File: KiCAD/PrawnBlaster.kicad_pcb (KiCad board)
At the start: 2 copper layers, 135 x 76.2 mm, 30 parts, among them J1 DB9_Female, J11 Flag_12, J14 Conn_01x03, J2 Flag_15, J5 Flag_14, J8 Flag_13, Q1 DMP6023LE, U1 78L05, U2 74ABT245

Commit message: Add 64Pin Case Power Supply, update PCB dimensions and SMA-Type
Note: Pi Pico footprint is missing!
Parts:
- removed H2: MountingHole, MountingHole:MountingHole_2.7mm_M2.5_DIN965
- removed J11: Flag_12, Connector_Coaxial:SMA_Amphenol_132134_Vertical
- removed J14: Conn_01x03, Connector:FanPinHeader_1x03_P2.54mm_Vertical
- removed J8: Flag_13, Connector_Coaxial:SMA_Amphenol_132134_Vertical
- added H4: MountingHole, MountingHole:MountingHole_2.7mm_M2.5_DIN965, F.Cu at (257.2, 42.0)
- added J3: Flag_14, Connector_Coaxial:SMA_Amphenol_132289_EdgeMount, F.Cu at (271.4, 20.6)
- added J4: Flag_13, Connector_Coaxial:SMA_Amphenol_132289_EdgeMount, F.Cu at (271.4, 32.8)
- added J6: C64AC, Custom_footprints_project:Socket_DIN41612-CaseC1-AC-Male-64Pin-2rows, F.Cu at (296.0, -37.6)
- added U2: SN74LV1T34DBV, Package_TO_SOT_SMD:SOT-23-5, F.Cu at (269.1, 41.2)
- J1: value DB9_Female -> Conn_Coaxial; footprint Connector_Dsub:DSUB-9_Female_Vertical_P2.77x2.84mm -> Connector_Coaxial:SMA_Amphenol_132289_EdgeMount
- J2: value Flag_15 -> Flag_12; footprint Connector_Coaxial:SMA_Amphenol_132134_Vertical -> Connector_Coaxial:SMA_Amphenol_132289_EdgeMount
- J5: value Flag_14 -> Flag_12; footprint Connector_Coaxial:SMA_Amphenol_132134_Vertical -> Connector_Coaxial:SMA_Amphenol_132289_EdgeMount
- moved J1 210.9 mm to (252.1, 20.6), turned to 0 degrees
- moved J5 162.9 mm to (290.7, 20.6)
- moved J2 116.1 mm to (252.1, 32.8)
- moved C1 57.4 mm to (76.7, -1.00)
- moved C2 57.4 mm to (76.7, 3.50)
- moved C3 57.4 mm to (77.7, 14.5)
- moved C4 57.4 mm to (76.7, 11.5)
- moved D1 57.4 mm to (84.7, 0.50)
- moved D2 57.4 mm to (70.2, 1.00)
- moved Q1 57.4 mm to (63.2, 1.50)
- moved R1 57.4 mm to (91.8, 25.4)
- moved R2 57.4 mm to (91.8, 22.9)
- moved R3 57.4 mm to (91.8, 20.4)
- moved R4 57.4 mm to (91.8, 17.9)
- moved R5 57.4 mm to (71.1, 4.00)
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- renumbered C5 to C4, H3 to H5, H4 to H7, R13 to R5, R14 to R6, R16 to R7, R18 to R8, R20 to R9, U1 to U3, U2 to U4
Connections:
- J1 pad 1: GND -> Net-(J1-Pad1)
- R1 pad 2: Net-(J11-Pad1) -> Net-(J5-Pad1)
- R3 pad 2: Net-(J5-Pad1) -> Net-(J3-Pad1)
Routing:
- net Net-(J2-Pad1): track 77.2 -> 0.00 mm
- net Net-(J5-Pad1): track 66.1 -> 0.00 mm
- net Net-(J6-Pad1): track 65.6 -> 0.00 mm, vias 2 -> 0
- net Net-(J4-Pad1): track 55.7 -> 0.00 mm
- net Net-(J9-Pad1): track 54.4 -> 0.00 mm
- net Net-(J3-Pad1): track 44.3 -> 0.00 mm
- net /Output Buffer/Vcc: track 109.9 -> 67.4 mm
- net /Output Buffer/A11: track 41.5 -> 0.00 mm
- net /Output Buffer/A10: track 41.1 -> 0.00 mm
- net /Output Buffer/A8: track 40.5 -> 0.00 mm
- net Net-(J11-Pad1): track 40.5 -> 0.00 mm
- net /Output Buffer/A9: track 40.1 -> 0.00 mm
- net Net-(J12-Pad1): track 38.8 -> 0.00 mm
- net /Output Buffer/A6: track 37.5 -> 0.00 mm
- net /Output Buffer/A4: track 37.3 -> 0.00 mm
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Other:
- board size 135 x 76.2 mm -> 160 x 100 mm
- board text removed: "1"
- board text removed: "2"
- board text removed: "3"
- board text removed: "8-18V"
- board text removed: "GND"
- board text removed: "NC"
- board text removed: "Pin"

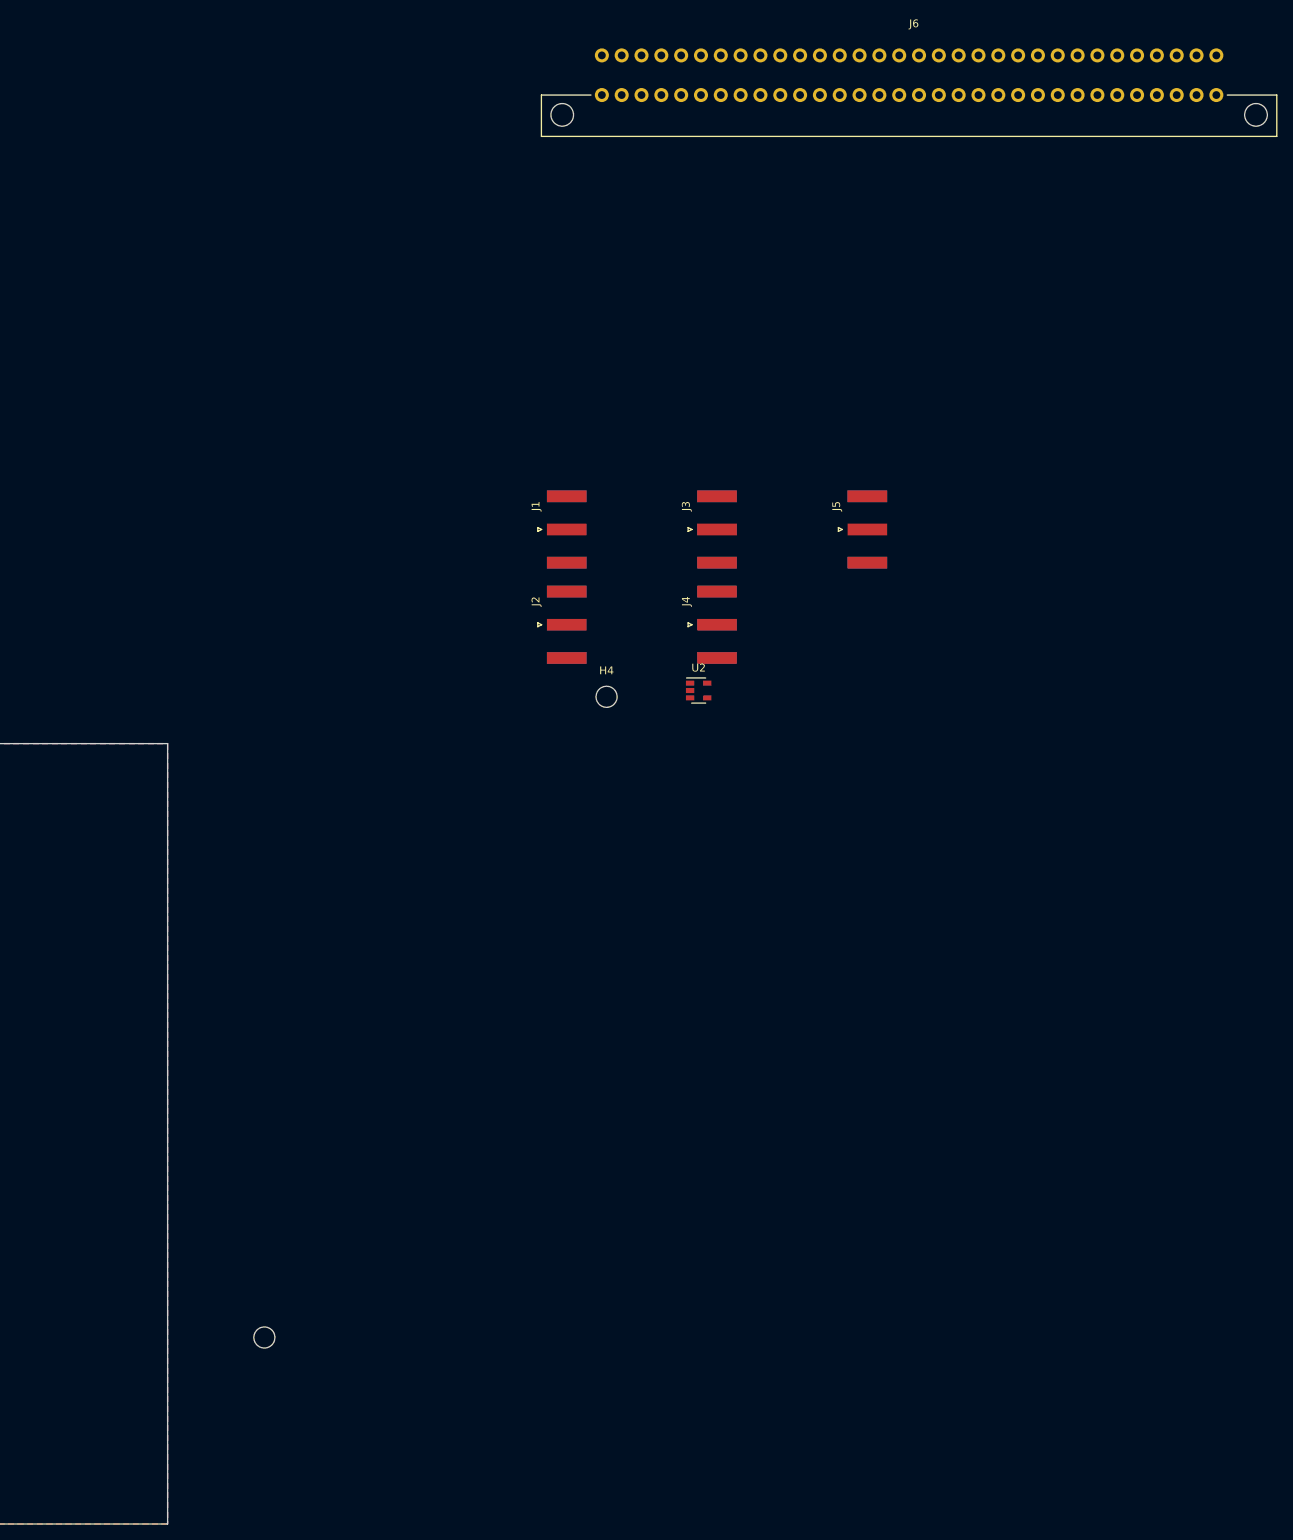
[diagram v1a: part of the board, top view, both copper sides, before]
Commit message: Place 64Pin Connector
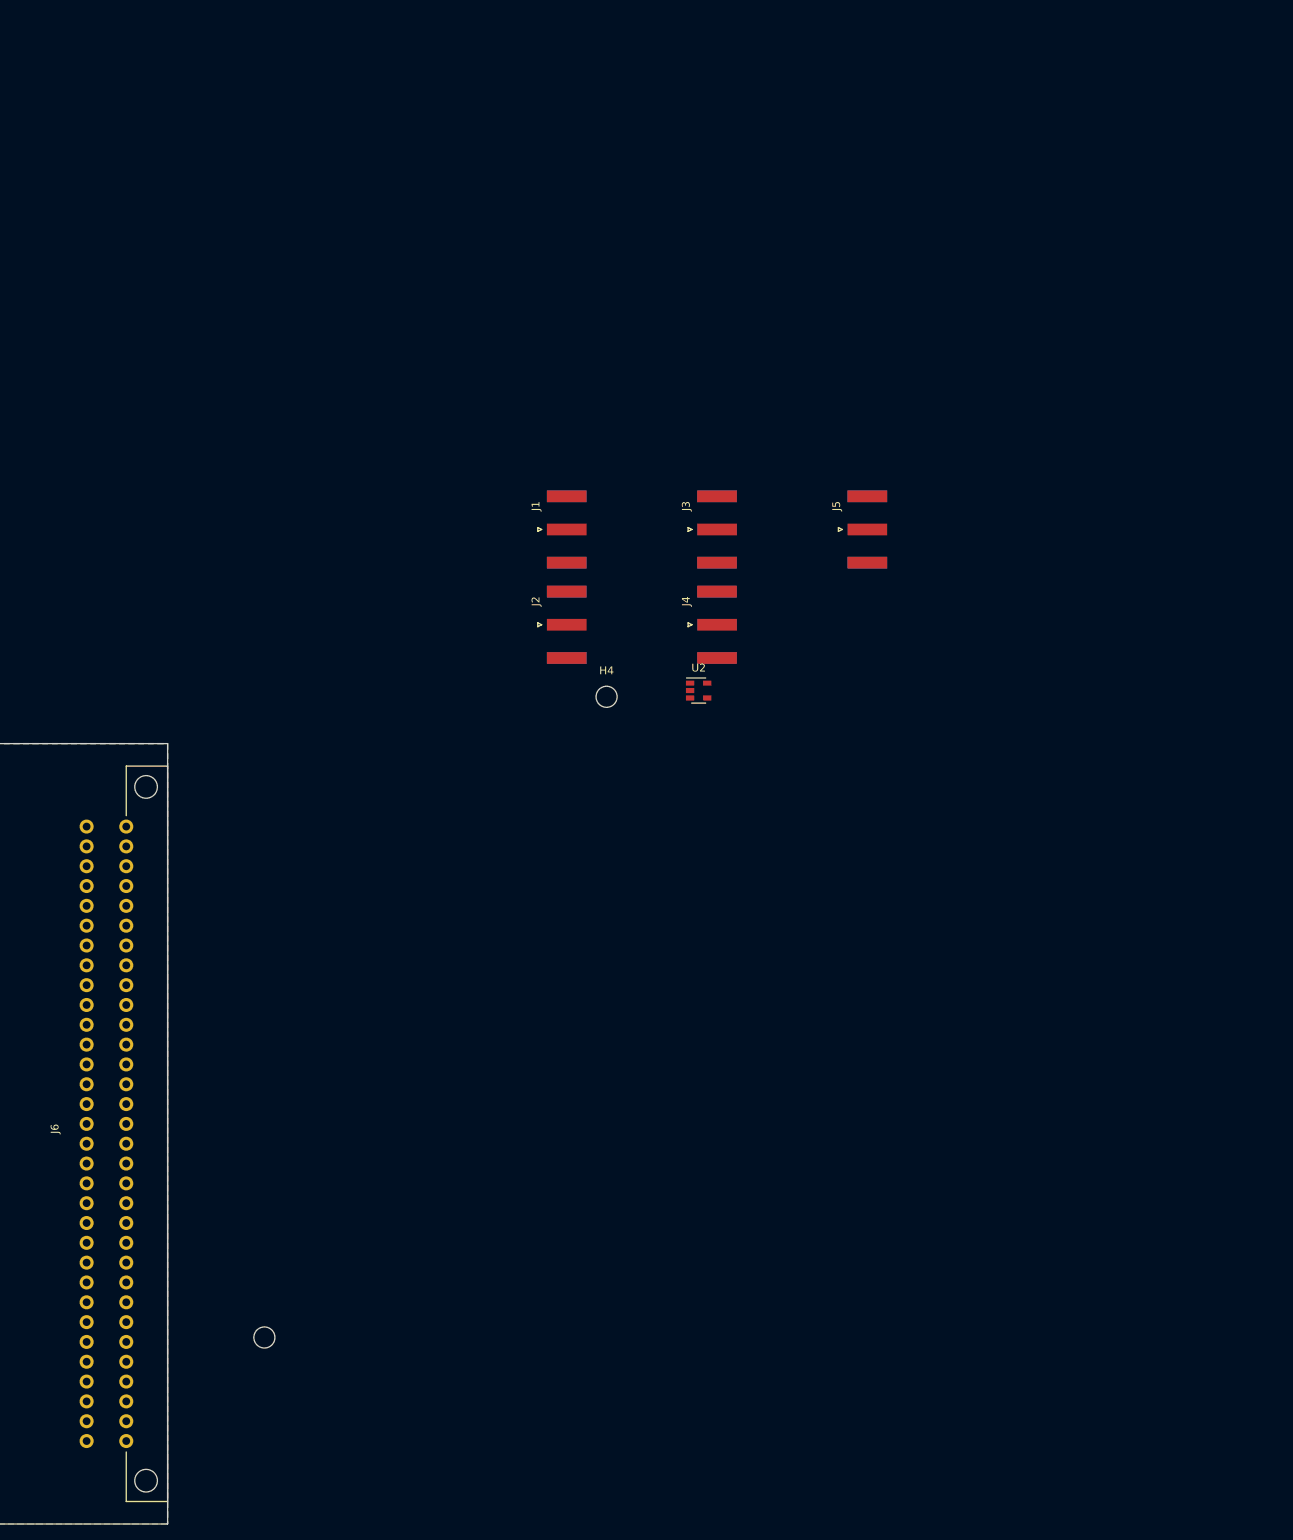
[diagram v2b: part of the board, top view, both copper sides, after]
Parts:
- moved J6 170.2 mm to (193.2, 98.0), turned to 90 degrees

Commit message: Add PiPico Footprint and route PCB without SMA connectors
Schematic was updated and routing on PCB was done except for input/output connectors.
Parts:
- added J10: Conn_01x20_Male, Connector_PinHeader_2.54mm:PinHeader_1x20_P2.54mm_Vertical, F.Cu at (118.2, 78.4)
- added J7: Conn_Coaxial, Connector_Coaxial:SMA_Amphenol_132289_EdgeMount, F.Cu at (46.9, 72.0)
- added J8: Conn_01x20_Male, Connector_PinHeader_2.54mm:PinHeader_1x20_P2.54mm_Vertical, F.Cu at (155.7, 126.6)
- added J9: Conn_01x03_Male, Connector_PinHeader_2.54mm:PinHeader_1x03_P2.54mm_Vertical, F.Cu at (134.3, 135.4)
- added U1: Pico, Custom_footprints_project:RPi_Pico_SMD_TH, F.Cu at (136.8, 102.5)
- added U5: SN74LV1T34DBV, Package_TO_SOT_SMD:SOT-23-5, F.Cu at (108.5, 72.7)
- moved J5 255.5 mm to (46.9, 97.0), turned to 180 degrees
- moved J3 246.5 mm to (46.8, 122.1), turned to 180 degrees
- moved J4 237.3 mm to (46.8, 109.3), turned to 180 degrees
- moved J2 230.2 mm to (47.0, 137.3), turned to 180 degrees
- moved J1 208.9 mm to (46.4, 56.8), turned to 180 degrees
- moved U2 164.6 mm to (108.5, 77.5)
- moved U3 143.7 mm to (180.5, 110.6), turned to 180 degrees
- moved C1 142.2 mm to (180.0, 96.6), turned to 0 degrees
- moved Q1 140.5 mm to (177.5, 83.1), turned to 90 degrees
- moved D1 140.2 mm to (178.5, 104.6), turned to 180 degrees
- moved D2 139.9 mm to (178.0, 90.1), turned to 180 degrees
- moved C2 135.8 mm to (175.5, 96.6), turned to 180 degrees
- moved R5 135.6 mm to (175.0, 91.0), turned to 270 degrees
- moved C4 117.2 mm to (93.5, 127.5), turned to 180 degrees
- moved R9 111.8 mm to (108.5, 120.2), turned to 0 degrees
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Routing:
- net Net-(J8-Pad6): track 0.00 -> 105.6 mm, vias 0 -> 1
- net /Output Buffer/Vcc: track 67.4 -> 154.4 mm
- net Net-(J8-Pad16): track 0.00 -> 80.3 mm
- net GND: track 11.3 -> 87.3 mm, vias 63 -> 8
- net /Power Supply/Reverse Polarity Protection/V18_unprot: track 8.65 -> 40.7 mm
- net /Output Buffer/A3: track 10.8 -> 32.3 mm
- net /Output Buffer/A0: track 10.6 -> 32.0 mm
- net /Output Buffer/A2: track 10.9 -> 31.1 mm
- net /Output Buffer/A1: track 10.5 -> 30.0 mm
- net Net-(J10-Pad1): track 0.00 -> 18.3 mm
- net Net-(J8-Pad9): track 0.00 -> 10.0 mm
- net Net-(J8-Pad7): track 0.00 -> 10.0 mm
- net Net-(J8-Pad5): track 0.00 -> 10.0 mm
- net Net-(J8-Pad4): track 0.00 -> 10.0 mm
- net Net-(J8-Pad20): track 0.00 -> 10.0 mm
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
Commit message: Exchange SMA-connectors with pin-header
Add pin Header to connect PCB with new Frontpanel PCB. Necessary distances marked. Routing finished.
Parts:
- removed J2, J5: Flag_12, Connector_Coaxial:SMA_Amphenol_132289_EdgeMount
- removed J3: Flag_14, Connector_Coaxial:SMA_Amphenol_132289_EdgeMount
- removed J4: Flag_13, Connector_Coaxial:SMA_Amphenol_132289_EdgeMount
- removed J7: Conn_Coaxial, Connector_Coaxial:SMA_Amphenol_132289_EdgeMount
- J1: value Conn_Coaxial -> Conn_02x06_Odd_Even; footprint Connector_Coaxial:SMA_Amphenol_132289_EdgeMount -> Connector_PinSocket_2.54mm:PinSocket_2x06_P2.54mm_Horizontal
- moved J1 20.0 mm to (58.2, 73.0), turned to 0 degrees
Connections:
- R1 pad 1: /Output Buffer/B3 -> /Output Buffer/B0
- R1 pad 2: Net-(J5-Pad1) -> Net-(J1-Pad5)
- R2 pad 1: /Output Buffer/B2 -> /Output Buffer/B1
- R2 pad 2: Net-(J4-Pad1) -> Net-(J1-Pad7)
- R3 pad 1: /Output Buffer/B1 -> /Output Buffer/B2
- R3 pad 2: Net-(J3-Pad1) -> Net-(J1-Pad9)
- R4 pad 1: /Output Buffer/B0 -> /Output Buffer/B3
- R4 pad 2: Net-(J2-Pad1) -> Net-(J1-Pad11)
- U2 pad 2: Net-(J1-Pad1) -> Net-(J1-Pad3)
- U5 pad 2: Net-(J7-Pad1) -> Net-(J1-Pad1)
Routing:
- net Net-(J1-Pad3): track 0.00 -> 50.0 mm
- net Net-(J1-Pad1): track 0.00 -> 49.4 mm
- net Net-(J1-Pad5): track 0.00 -> 43.5 mm
- net Net-(J1-Pad7): track 0.00 -> 43.5 mm
- net Net-(J1-Pad9): track 0.00 -> 43.5 mm
- net Net-(J1-Pad11): track 0.00 -> 43.4 mm
- net /Output Buffer/A1: track 30.0 -> 20.4 mm
- net /Output Buffer/A0: track 32.0 -> 23.0 mm
- net /Output Buffer/A3: track 32.3 -> 24.6 mm
- net /Output Buffer/A2: track 31.1 -> 25.5 mm
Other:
- board text added: "Inner board edge"

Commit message: Finish routing PCB
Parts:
- removed H1, H4, H5, H7: MountingHole, MountingHole:MountingHole_2.7mm_M2.5_DIN965
- added C5: 100n, Capacitor_SMD:C_0603_1608Metric, F.Cu at (108.2, 74.3)
- added C6: 10u, Capacitor_SMD:C_1210_3225Metric, F.Cu at (110.6, 75.0)
- moved LOGO1 43.0 mm to (176.8, 54.3)
- moved LOGO2 43.0 mm to (166.3, 54.4)
- moved U2 4.60 mm to (103.9, 77.5)
- moved U5 4.60 mm to (103.9, 72.7)
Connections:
- R1 pad 1: /Output Buffer/B0 -> /Output Buffer/B3
- R2 pad 1: /Output Buffer/B1 -> /Output Buffer/B2
- R3 pad 1: /Output Buffer/B2 -> /Output Buffer/B1
- R4 pad 1: /Output Buffer/B3 -> /Output Buffer/B0
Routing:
- net /Output Buffer/A1: track 20.4 -> 30.0 mm
- net /Output Buffer/A0: track 23.0 -> 32.0 mm
- net /Output Buffer/A3: track 24.6 -> 32.3 mm
- net /Output Buffer/A2: track 25.5 -> 31.1 mm
- net Net-(C5-Pad1): track 80.3 -> 85.1 mm
- net Net-(J8-Pad6): track 105.6 -> 110.3 mm
- net Net-(J1-Pad3): track 50.0 -> 45.4 mm
- net Net-(J1-Pad1): track 49.4 -> 44.8 mm
- net Net-(J10-Pad1): track 18.3 -> 22.9 mm
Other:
- board text added: "Prawnblaster Breakout Design: Lars Pause Date: 2021-10 Version: 1.0"
- board text removed: "Pulseblaster Flag 12 to 23 Breakout Design: Patrick Baus / Lars Pause Date: 2020-12 Version: 1.0"

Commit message: Small updates
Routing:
- net Net-(J8-Pad6): track 110.3 -> 105.4 mm, vias 1 -> 9
- net GND: track 87.3 -> 86.5 mm, vias 8 -> 543
- net Net-(J8-Pad9): vias 0 -> 1
- net Net-(J8-Pad7): vias 0 -> 1
- net Net-(J8-Pad5): vias 0 -> 1
- net Net-(J8-Pad19): vias 0 -> 2
- net Net-(J8-Pad17): vias 0 -> 2
- net Net-(J8-Pad15): vias 0 -> 2
- net Net-(J8-Pad13): vias 0 -> 1
- net Net-(J8-Pad11): vias 0 -> 1
- net Net-(J8-Pad1): vias 0 -> 1
- net Net-(J10-Pad6): vias 0 -> 1
- net Net-(J10-Pad4): vias 0 -> 1
- net Net-(J10-Pad2): vias 0 -> 1
- net Net-(J1-Pad9): vias 0 -> 3
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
